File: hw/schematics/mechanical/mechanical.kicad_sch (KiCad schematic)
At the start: 5 parts

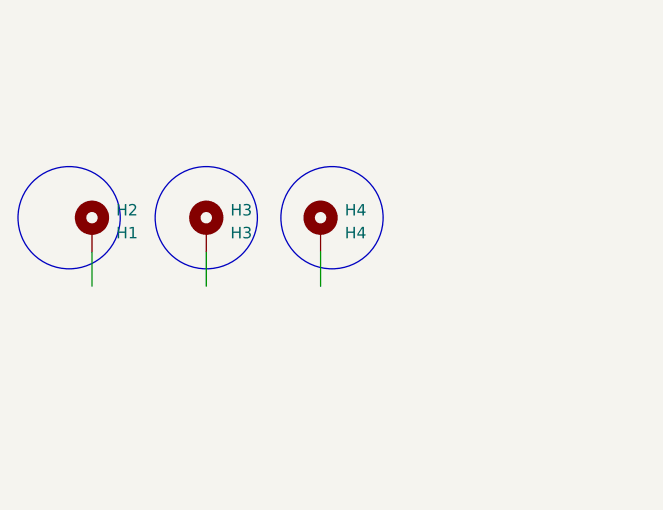
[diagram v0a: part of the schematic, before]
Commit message: 
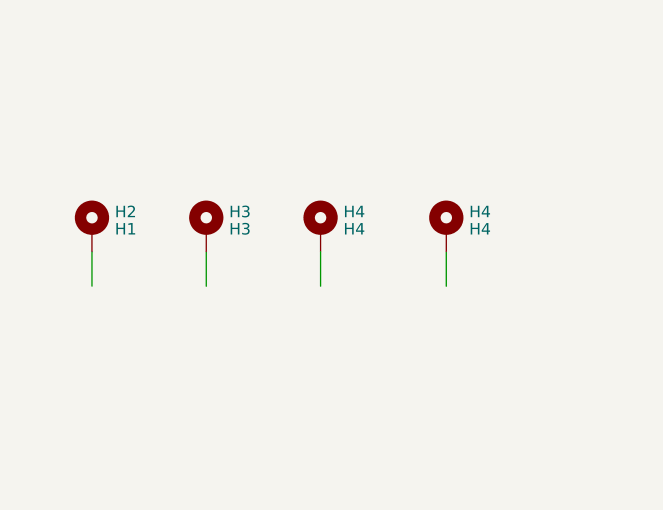
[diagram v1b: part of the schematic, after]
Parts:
- added H4: H4, MountingHole:MountingHole_2.2mm_M2_Pad, symbol Mechanical:MountingHole_Pad
- H2, H3, H4: footprint MountingHole:MountingHole_2.5mm_Pad -> MountingHole:MountingHole_2.2mm_M2_Pad
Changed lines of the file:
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@@
 (kicad_sch (version 20230121) (generator eeschema)
   (paper "A4")
+  (wire (pts (xy 138.43 60.96) (xy 138.43 64.77))
+    (stroke (width 0) (type default))
+  )
   (wire (pts (xy 124.46 60.96) (xy 124.46 64.77))
     (stroke (width 0) (type default))
@@
   (wire (pts (xy 111.76 60.96) (xy 111.76 64.77))
     (stroke (width 0) (type default))
-  )
-  (circle (center 125.73 57.15) (radius 5.6796)
-    (stroke (width 0) (type default) (color 255 0 0 1))
-    (fill (type none))
   )
   (circle (center 203.2 40.64) (radius 5.6796)
@@
     (fill (type none))
   )
-  (circle (center 96.52 57.15) (radius 5.6796)
-    (stroke (width 0) (type default) (color 255 0 0 1))
-    (fill (type none))
-  )
-  (circle (center 111.76 57.15) (radius 5.6796)
-    (stroke (width 0) (type default) (color 255 0 0 1))
-    (fill (type none))
-  )
   (circle (center 254 49.53) (radius 5.6796)
     (stroke (width 0) (type default) (color 255 0 0 1))
     (fill (type none))
   )
+  (symbol (lib_id "Mechanical:MountingHole_Pad") (at 138.43 58.42 0) (unit 1)
+    (in_bom yes) (on_board yes) (dnp no) (fields_autoplaced)
+    (property "Reference" "H4" (at 140.97 56.5063 0)
+      (effects (font (size 1.27 1.27)) (justify left))
+    )
+    (property "Value" "H4" (at 140.97 58.4273 0)
+      (effects (font (size 1.27 1.27)) (justify left))
+    )
+    (property "Footprint" "MountingHole:MountingHole_2.2mm_M2_Pad" (at 138.43 58.42 0)
+      (effects (font (size 1.27 1.27)) hide)
+    )
+    (property "Datasheet" "~" (at 138.43 58.42 0)
+      (effects (font (size 1.27 1.27)) hide)
+    )
+    (pin "1")
+    (instances
+      (project "friendly-keyboard"
+        (path "/facac7ae-a8b7-40c9-80fb-c9ce3ae3187a"
+          (reference "H4") (unit 1)
+        )
+        (path "/facac7ae-a8b7-40c9-80fb-c9ce3ae3187a/b9a80e9a-69d8-419d-bf29-e4473804ac8b"
+          (reference "H4") (unit 1)
+        )
+      )
+    )
+  )
   (symbol (lib_id "Mechanical:MountingHole_Pad") (at 111.76 58.42 0) (unit 1)
     (in_bom yes) (on_board yes) (dnp no) (fields_autoplaced)
-    (property "Reference" "H3" (at 115.6494 56.3153 0)
-      (effects (font (size 1.27 1.27)))
-    )
-    (property "Value" "H3" (at 115.6494 58.8522 0)
-      (effects (font (size 1.27 1.27)))
-    )
-    (property "Footprint" "MountingHole:MountingHole_2.5mm_Pad" (at 111.76 58.42 0)
+    (property "Reference" "H3" (at 114.3 56.5063 0)
+      (effects (font (size 1.27 1.27)) (justify left))
+    )
+    (property "Value" "H3" (at 114.3 58.4273 0)
+      (effects (font (size 1.27 1.27)) (justify left))
+    )
+    (property "Footprint" "MountingHole:MountingHole_2.2mm_M2_Pad" (at 111.76 58.42 0)
       (effects (font (size 1.27 1.27)) hide)
     )
@@
         )
         (path "/facac7ae-a8b7-40c9-80fb-c9ce3ae3187a/b9a80e9a-69d8-419d-bf29-e4473804ac8b"
-          (reference "H?") (unit 1)
+          (reference "H2") (unit 1)
         )
       )
@@
   (symbol (lib_id "Mechanical:MountingHole_Pad") (at 99.06 58.42 0) (unit 1)
     (in_bom yes) (on_board yes) (dnp no) (fields_autoplaced)
-    (property "Reference" "H2" (at 102.9494 56.3153 0)
-      (effects (font (size 1.27 1.27)))
-    )
-    (property "Value" "H1" (at 102.9494 58.8522 0)
-      (effects (font (size 1.27 1.27)))
-    )
-    (property "Footprint" "MountingHole:MountingHole_2.5mm_Pad" (at 99.06 58.42 0)
+    (property "Reference" "H2" (at 101.6 56.5063 0)
+      (effects (font (size 1.27 1.27)) (justify left))
+    )
+    (property "Value" "H1" (at 101.6 58.4273 0)
+      (effects (font (size 1.27 1.27)) (justify left))
+    )
+    (property "Footprint" "MountingHole:MountingHole_2.2mm_M2_Pad" (at 99.06 58.42 0)
       (effects (font (size 1.27 1.27)) hide)
     )
@@
         )
         (path "/facac7ae-a8b7-40c9-80fb-c9ce3ae3187a/b9a80e9a-69d8-419d-bf29-e4473804ac8b"
-          (reference "H?") (unit 1)
+          (reference "H1") (unit 1)
         )
       )
@@
         )
         (path "/facac7ae-a8b7-40c9-80fb-c9ce3ae3187a/b9a80e9a-69d8-419d-bf29-e4473804ac8b"
-          (reference "J?") (unit 1)
+          (reference "J4") (unit 1)
         )
       )
@@
   (symbol (lib_id "Mechanical:MountingHole_Pad") (at 124.46 58.42 0) (unit 1)
     (in_bom yes) (on_board yes) (dnp no) (fields_autoplaced)
-    (property "Reference" "H4" (at 128.3494 56.3153 0)
-      (effects (font (size 1.27 1.27)))
-    )
-    (property "Value" "H4" (at 128.3494 58.8522 0)
-      (effects (font (size 1.27 1.27)))
-    )
-    (property "Footprint" "MountingHole:MountingHole_2.5mm_Pad" (at 124.46 58.42 0)
+    (property "Reference" "H4" (at 127 56.5063 0)
+      (effects (font (size 1.27 1.27)) (justify left))
+    )
+    (property "Value" "H4" (at 127 58.4273 0)
+      (effects (font (size 1.27 1.27)) (justify left))
+    )
+    (property "Footprint" "MountingHole:MountingHole_2.2mm_M2_Pad" (at 124.46 58.42 0)
       (effects (font (size 1.27 1.27)) hide)
     )
@@
         )
         (path "/facac7ae-a8b7-40c9-80fb-c9ce3ae3187a/b9a80e9a-69d8-419d-bf29-e4473804ac8b"
-          (reference "H?") (unit 1)
+          (reference "H3") (unit 1)
         )
       )
@@
         )
         (path "/facac7ae-a8b7-40c9-80fb-c9ce3ae3187a/b9a80e9a-69d8-419d-bf29-e4473804ac8b"
-          (reference "J?") (unit 1)
-        )
-      )
+          (reference "J5") (unit 1)
+        )
+      )
